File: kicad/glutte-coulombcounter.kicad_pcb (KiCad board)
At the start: 2 copper layers, 100 x 85 mm, 72 parts, among them J1 12V, J2 Measure, J3 K1, J4 AVR-ISP-6, J5 Glutte, J6 K2, J7 K3, J8 Raspi, K1 G6SK-2F-DC5, K2 G6SK-2F-DC5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

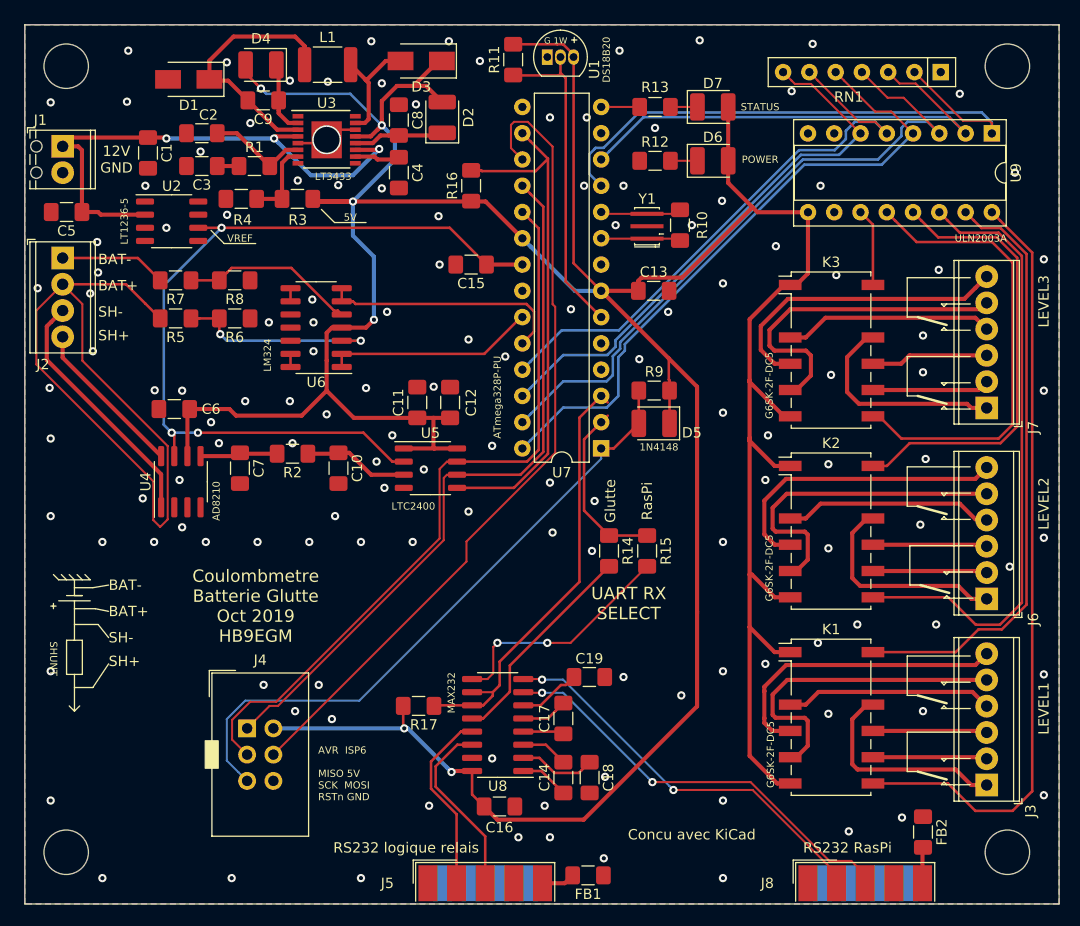
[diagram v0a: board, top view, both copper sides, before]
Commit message: Change R and C to 0805, improve silkscreen
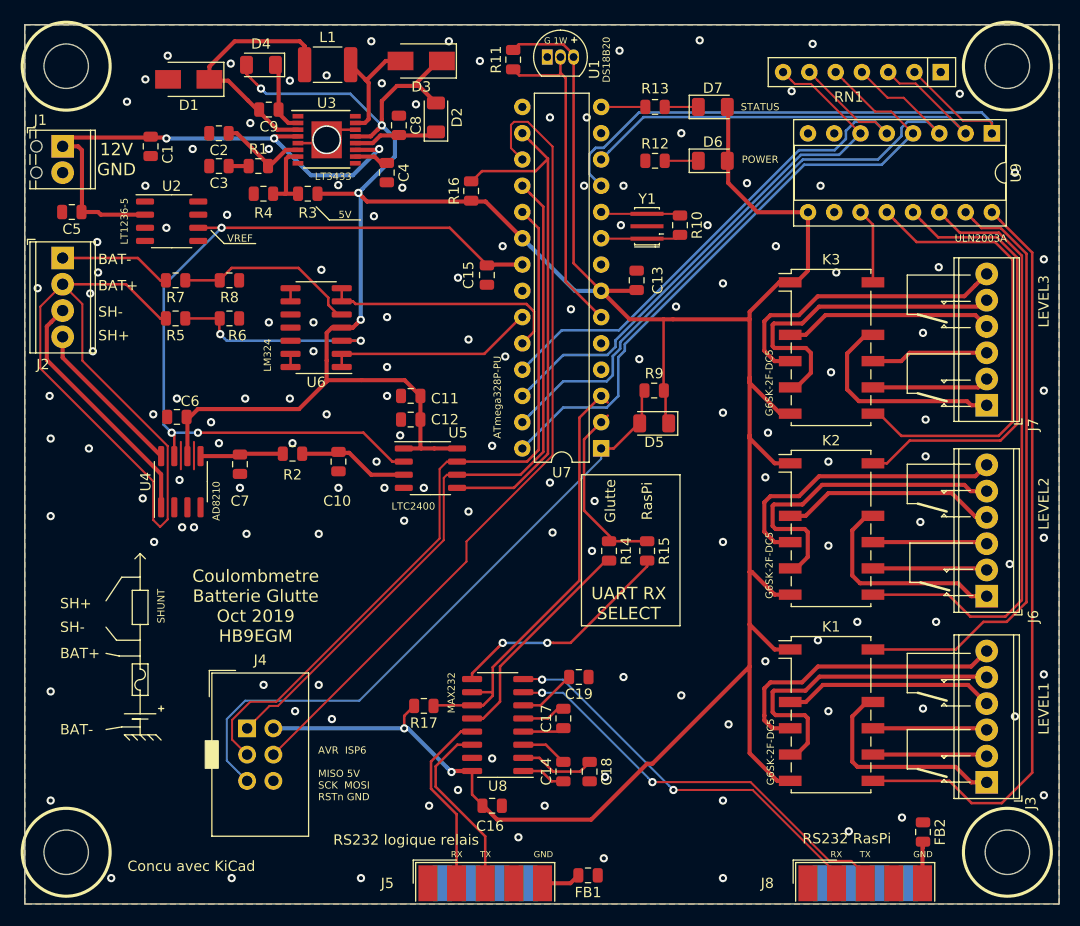
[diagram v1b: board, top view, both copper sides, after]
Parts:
- C1, C10, C11, C12, C13, C14, C15, C16, C17, C18, C19, C2, C3, C4, C5, C6, C7, C8, C9: footprint Capacitor_SMD:C_1206_3216Metric_Pad1.42x1.75mm_HandSolder -> Capacitor_SMD:C_0805_2012Metric
- D2, D4, D5: footprint Diode_SMD:D_1210_3225Metric_Pad1.42x2.65mm_HandSolder -> Diode_SMD:D_1206_3216Metric
- D6, D7: footprint LED_SMD:LED_1210_3225Metric_Pad1.42x2.65mm_HandSolder -> LED_SMD:LED_1206_3216Metric
- FB1, FB2: footprint Resistor_SMD:R_1206_3216Metric_Pad1.42x1.75mm_HandSolder -> Inductor_SMD:L_0805_2012Metric
- R1, R10, R11, R12, R13, R14, R15, R16, R17, R2, R3, R4, R5, R6, R7, R8, R9: footprint Resistor_SMD:R_1206_3216Metric_Pad1.42x1.75mm_HandSolder -> Resistor_SMD:R_0805_2012Metric
- moved C12 4.15 mm to (67.3, 58.2), turned to 180 degrees
- moved R4 2.20 mm to (53.1, 36.3)
- moved C13 1.94 mm to (89.2, 44.7), turned to 90 degrees
- moved C15 1.83 mm to (74.7, 44.2), turned to 270 degrees
- moved C2 1.65 mm to (48.8, 30.5)
- moved C3 1.65 mm to (48.8, 33.7)
- moved C4 1.17 mm to (65.0, 34.3)
- moved R3 1.12 mm to (57.4, 36.3)
- moved C9 1.04 mm to (53.6, 28.2)
- moved C19 1.02 mm to (83.6, 83.1)
- moved C11 0.90 mm to (67.3, 55.9), turned to 180 degrees
- moved C6 0.80 mm to (44.7, 57.9)
- moved C16 0.71 mm to (75.2, 95.5)
- moved C1 0.68 mm to (42.2, 31.8)
- moved C10 0.64 mm to (60.3, 62.2)
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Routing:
- net +5VA: track 390.6 -> 348.2 mm
- net GNDA: track 6.09 -> 11.4 mm, vias 135 -> 138
- net Net-(K1-Pad7): track 74.9 -> 73.3 mm
- net Net-(C4-Pad1): track 4.42 -> 3.30 mm
- net Net-(C2-Pad1): track 9.77 -> 8.66 mm
- net Net-(FB2-Pad2): track 3.49 -> 4.59 mm
- net Net-(C9-Pad1): track 8.04 -> 7.06 mm
- net Net-(R7-Pad1): track 16.9 -> 17.9 mm
- net VREF: track 81.2 -> 82.0 mm
- net Net-(R14-Pad2): track 20.8 -> 21.6 mm
- net Net-(C9-Pad2): track 24.7 -> 24.0 mm
- net Net-(K2-Pad7): track 59.6 -> 59.0 mm
- net Net-(R3-Pad1): track 7.72 -> 7.06 mm
- net Net-(J6-Pad4): track 20.3 -> 20.9 mm
- net Net-(R15-Pad2): track 22.9 -> 22.3 mm
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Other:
- board text added: "GND"
- board text added: "RX"
- board text added: "TX"
